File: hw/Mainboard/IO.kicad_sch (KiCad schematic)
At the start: 11 parts, among them U11 W65C21N, U12 W65C22N, U13 W65C21N

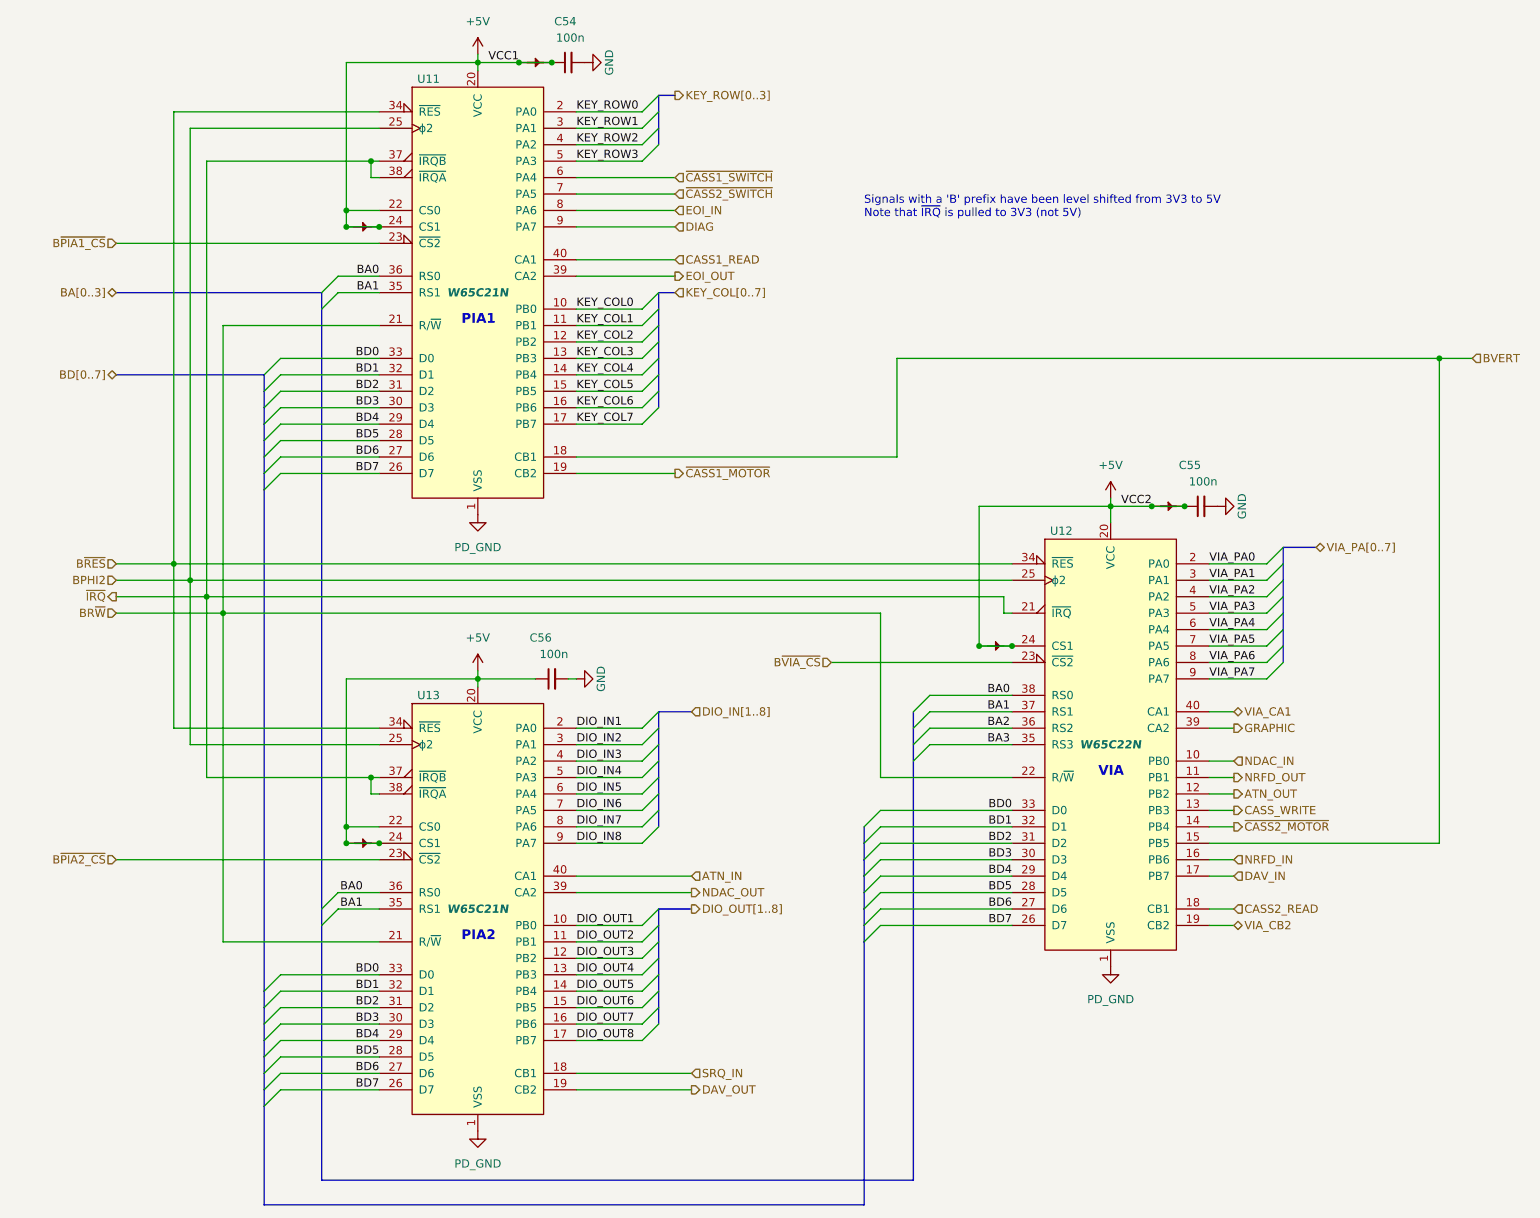
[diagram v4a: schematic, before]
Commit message: hw: remove net/power ties
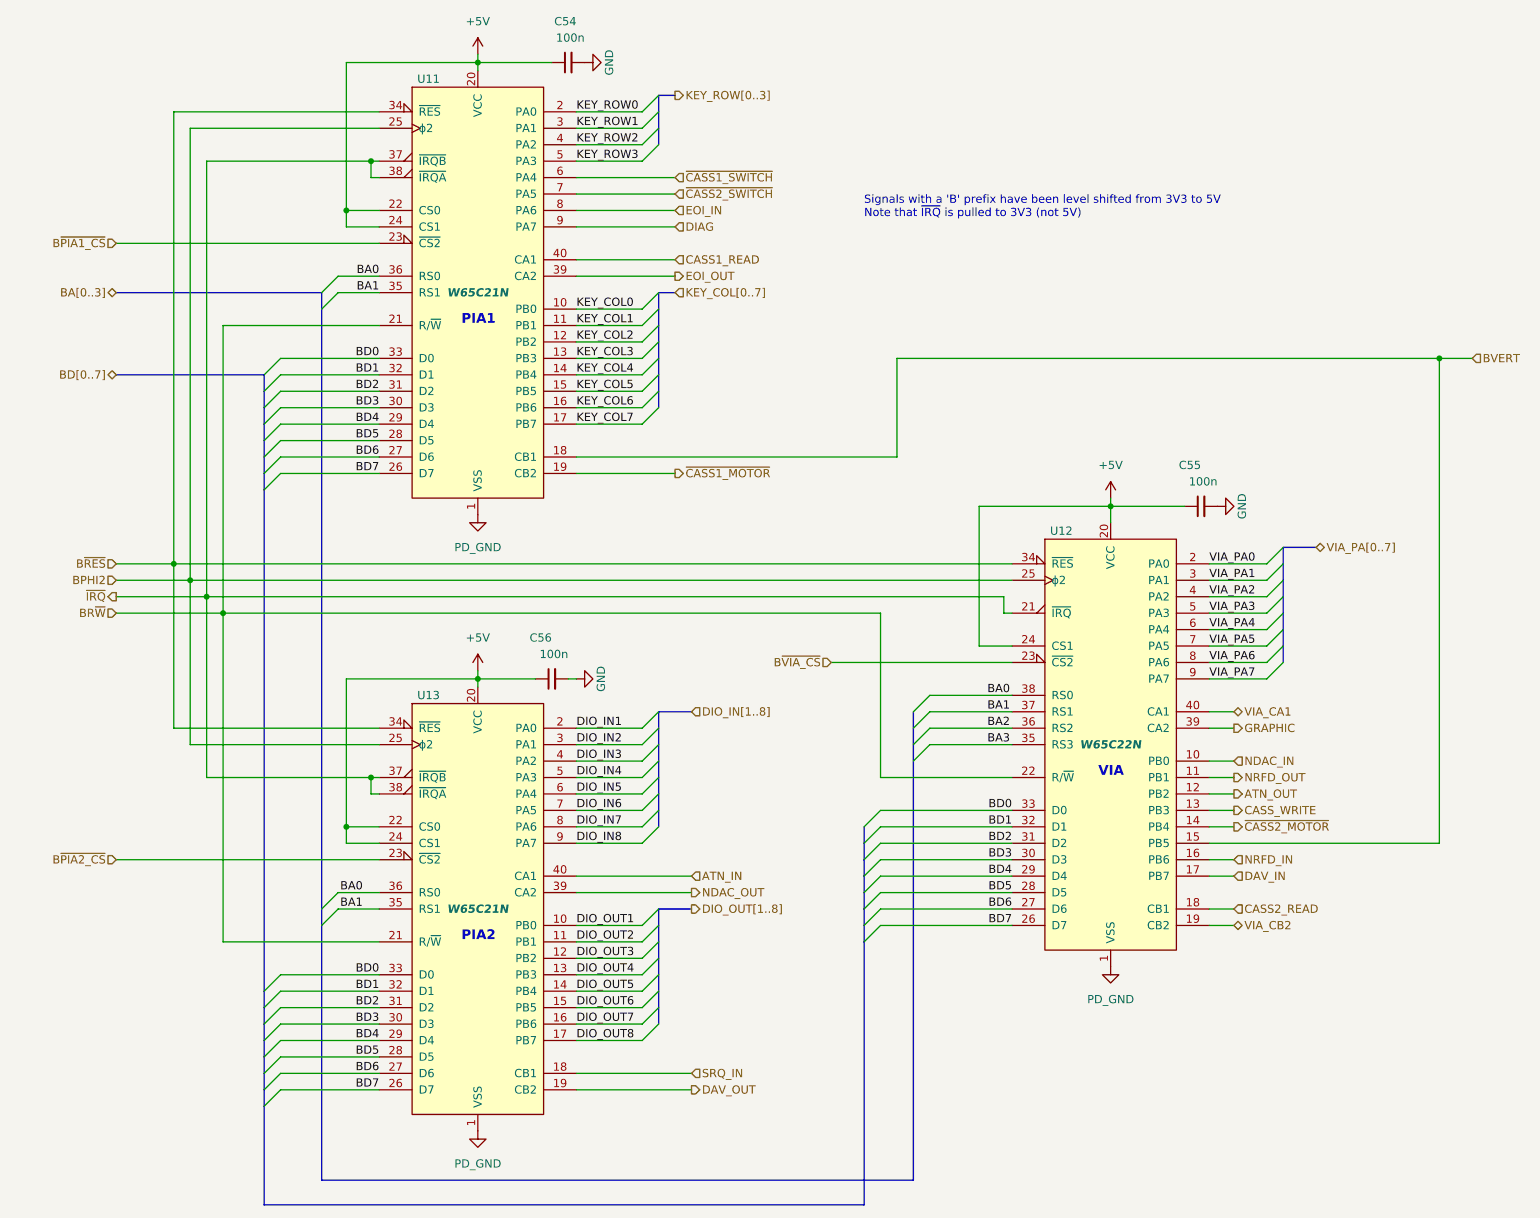
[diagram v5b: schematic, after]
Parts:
- removed PT31, PT32, PT33, PT34, PT35: PowerTie_2, PET:NetTie-2_SMD_Pad_1.6_to_0.4mm, symbol PET:PowerTie_2
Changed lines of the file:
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@@
   (junction (at 66.04 140.97) (diameter 0) (color 0 0 0 0)
   )
-  (junction (at 97.79 22.86) (diameter 0) (color 0 0 0 0)
-  )
-  (junction (at 71.12 48.26) (diameter 0) (color 0 0 0 0)
-  )
   (junction (at 184.15 91.44) (diameter 0) (color 0 0 0 0)
   )
-  (junction (at 92.71 22.86) (diameter 0) (color 0 0 0 0)
-  )
-  (junction (at 66.04 48.26) (diameter 0) (color 0 0 0 0)
-  )
   (junction (at 86.36 22.86) (diameter 0) (color 0 0 0 0)
   )
-  (junction (at 168.91 113.03) (diameter 0) (color 0 0 0 0)
-  )
   (junction (at 86.36 118.11) (diameter 0) (color 0 0 0 0)
   )
-  (junction (at 71.12 143.51) (diameter 0) (color 0 0 0 0)
-  )
   (junction (at 69.85 133.35) (diameter 0) (color 0 0 0 0)
   )
@@
   (junction (at 234.95 68.58) (diameter 0) (color 0 0 0 0)
   )
-  (junction (at 195.58 91.44) (diameter 0) (color 0 0 0 0)
-  )
   (junction (at 41.91 102.87) (diameter 0) (color 0 0 0 0)
   )
-  (junction (at 163.83 113.03) (diameter 0) (color 0 0 0 0)
-  )
   (junction (at 66.04 45.72) (diameter 0) (color 0 0 0 0)
   )
-  (junction (at 66.04 143.51) (diameter 0) (color 0 0 0 0)
-  )
   (junction (at 46.99 107.95) (diameter 0) (color 0 0 0 0)
   )
-  (junction (at 190.5 91.44) (diameter 0) (color 0 0 0 0)
-  )
   (junction (at 39.37 100.33) (diameter 0) (color 0 0 0 0)
   )
@@
     (stroke (width 0) (type default) (color 0 0 0 0))
   )
-  (wire (pts (xy 86.36 22.86) (xy 92.71 22.86))
+  (wire (pts (xy 86.36 22.86) (xy 97.79 22.86))
     (stroke (width 0) (type default) (color 0 0 0 0))
   )
@@
     (stroke (width 0) (type default) (color 0 0 0 0))
   )
-  (wire (pts (xy 190.5 91.44) (xy 184.15 91.44))
+  (wire (pts (xy 184.15 91.44) (xy 195.58 91.44))
     (stroke (width 0) (type default) (color 0 0 0 0))
   )
@@
     (stroke (width 0) (type default) (color 0 0 0 0))
   )
-  (wire (pts (xy 92.71 22.86) (xy 97.79 22.86))
-    (stroke (width 0) (type default) (color 0 0 0 0))
-  )
   (wire (pts (xy 55.88 166.37) (xy 71.12 166.37))
     (stroke (width 0) (type default) (color 0 0 0 0))
@@
   )
   (bus (pts (xy 210.82 102.87) (xy 210.82 105.41))
-    (stroke (width 0) (type default) (color 0 0 0 0))
-  )
-  (wire (pts (xy 190.5 91.44) (xy 195.58 91.44))
     (stroke (width 0) (type default) (color 0 0 0 0))
   )
@@
     (effects (font (size 1.27 1.27)) (justify right bottom))
   )
-  (label "VCC2" (at 190.5 91.44 180)
-    (effects (font (size 1.27 1.27)) (justify right bottom))
-  )
   (label "BD2" (at 168.91 143.51 180)
     (effects (font (size 1.27 1.27)) (justify right bottom))
@@
   (label "DIO_IN4" (at 101.6 133.35 0)
     (effects (font (size 1.27 1.27)) (justify left bottom))
-  )
-  (label "VCC1" (at 92.71 22.86 180)
-    (effects (font (size 1.27 1.27)) (justify right bottom))
   )
   (label "BD4" (at 168.91 148.59 180)
@@
     (pin "1")
   )
-  (symbol (lib_id "PET:PowerTie_2") (at 95.25 22.86 0) (unit 1)
-    (in_bom yes) (on_board yes) (fields_autoplaced)
-    (property "Reference" "PT31" (id 0) (at 95.25 20.955 0)
-      (effects (font (size 1.27 1.27)) hide)
-    )
-    (property "Value" "PowerTie_2" (id 1) (at 95.25 24.765 0)
-      (effects (font (size 1.27 1.27)) hide)
-    )
-    (property "Footprint" "PET:NetTie-2_SMD_Pad_1.6_to_0.4mm" (id 2) (at 95.25 22.86 0)
-      (effects (font (size 1.27 1.27)) hide)
-    )
-    (property "Datasheet" "~" (id 3) (at 95.25 22.86 0)
-      (effects (font (size 1.27 1.27)) hide)
-    )
-    (pin "1")
-    (pin "2")
-  )
-  (symbol (lib_id "PET:PowerTie_2") (at 68.58 143.51 0) (unit 1)
-    (in_bom yes) (on_board yes) (fields_autoplaced)
-    (property "Reference" "PT35" (id 0) (at 68.58 141.605 0)
-      (effects (font (size 1.27 1.27)) hide)
-    )
-    (property "Value" "PowerTie_2" (id 1) (at 68.58 145.415 0)
-      (effects (font (size 1.27 1.27)) hide)
-    )
-    (property "Footprint" "PET:NetTie-2_SMD_Pad_1.6_to_0.4mm" (id 2) (at 68.58 143.51 0)
-      (effects (font (size 1.27 1.27)) hide)
-    )
-    (property "Datasheet" "~" (id 3) (at 68.58 143.51 0)
-      (effects (font (size 1.27 1.27)) hide)
-    )
-    (pin "1")
-    (pin "2")
-  )
-  (symbol (lib_id "PET:PowerTie_2") (at 166.37 113.03 0) (unit 1)
-    (in_bom yes) (on_board yes) (fields_autoplaced)
-    (property "Reference" "PT34" (id 0) (at 166.37 111.125 0)
-      (effects (font (size 1.27 1.27)) hide)
-    )
-    (property "Value" "PowerTie_2" (id 1) (at 166.37 114.935 0)
-      (effects (font (size 1.27 1.27)) hide)
-    )
-    (property "Footprint" "PET:NetTie-2_SMD_Pad_1.6_to_0.4mm" (id 2) (at 166.37 113.03 0)
-      (effects (font (size 1.27 1.27)) hide)
-    )
-    (property "Datasheet" "~" (id 3) (at 166.37 113.03 0)
-      (effects (font (size 1.27 1.27)) hide)
-    )
-    (pin "1")
-    (pin "2")
-  )
-  (symbol (lib_id "PET:PowerTie_2") (at 193.04 91.44 0) (unit 1)
-    (in_bom yes) (on_board yes) (fields_autoplaced)
-    (property "Reference" "PT33" (id 0) (at 193.04 89.535 0)
-      (effects (font (size 1.27 1.27)) hide)
-    )
-    (property "Value" "PowerTie_2" (id 1) (at 193.04 93.345 0)
-      (effects (font (size 1.27 1.27)) hide)
-    )
-    (property "Footprint" "PET:NetTie-2_SMD_Pad_1.6_to_0.4mm" (id 2) (at 193.04 91.44 0)
-      (effects (font (size 1.27 1.27)) hide)
-    )
-    (property "Datasheet" "~" (id 3) (at 193.04 91.44 0)
-      (effects (font (size 1.27 1.27)) hide)
-    )
-    (pin "1")
-    (pin "2")
-  )
   (symbol (lib_id "power:GND") (at 102.87 22.86 90) (unit 1)
     (in_bom yes) (on_board yes)
@@
     (pin "1")
   )
-  (symbol (lib_id "PET:PowerTie_2") (at 68.58 48.26 0) (unit 1)
-    (in_bom yes) (on_board yes) (fields_autoplaced)
-    (property "Reference" "PT32" (id 0) (at 68.58 46.355 0)
-      (effects (font (size 1.27 1.27)) hide)
-    )
-    (property "Value" "PowerTie_2" (id 1) (at 68.58 50.165 0)
-      (effects (font (size 1.27 1.27)) hide)
-    )
-    (property "Footprint" "PET:NetTie-2_SMD_Pad_1.6_to_0.4mm" (id 2) (at 68.58 48.26 0)
-      (effects (font (size 1.27 1.27)) hide)
-    )
-    (property "Datasheet" "~" (id 3) (at 68.58 48.26 0)
-      (effects (font (size 1.27 1.27)) hide)
-    )
-    (pin "1")
-    (pin "2")
-  )
   (symbol (lib_id "power:+5V") (at 184.15 90.17 0) (unit 1)
